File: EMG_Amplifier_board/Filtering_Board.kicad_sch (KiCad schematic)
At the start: 3 parts, among them U7 TPD2E001DRLR

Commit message: pcb design v1
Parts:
- removed R17, R18: 10R, Resistor_SMD:R_0402_1005Metric, symbol Device:R
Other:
- sheet DRL ports: added none; removed V_DD/2

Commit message: add capacitor to ESD
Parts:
- added C12: 0.1uF, Capacitor_SMD:C_0805_2012Metric, symbol Device:C_Small
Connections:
- net +V_DD: now also C12.2
- net GND: now also C12.1
- no-connect marks 0 -> 1
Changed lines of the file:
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@@
 		(color 0 0 0 0)
 	)
+	(junction
+		(at 110.49 152.4)
+		(diameter 0)
+		(color 0 0 0 0)
+	)
+	(no_connect
+		(at 101.6 142.24)
+	)
 	(wire
 		(pts
@@
 	(wire
 		(pts
+			(xy 110.49 154.94) (xy 110.49 152.4)
+		)
+		(stroke
+			(width 0)
+			(type default)
+		)
+	)
+	(wire
+		(pts
 			(xy 255.27 50.8) (xy 255.27 118.11)
 		)
@@
 	(wire
 		(pts
+			(xy 110.49 152.4) (xy 99.06 152.4)
+		)
+		(stroke
+			(width 0)
+			(type default)
+		)
+	)
+	(wire
+		(pts
 			(xy 163.83 45.72) (xy 121.92 45.72)
 		)
@@
 	(wire
 		(pts
+			(xy 110.49 160.02) (xy 110.49 161.29)
+		)
+		(stroke
+			(width 0)
+			(type default)
+		)
+	)
+	(wire
+		(pts
 			(xy 163.83 36.83) (xy 163.83 45.72)
 		)
@@
 	(wire
 		(pts
-			(xy 121.92 152.4) (xy 99.06 152.4)
+			(xy 121.92 152.4) (xy 110.49 152.4)
 		)
 		(stroke
@@
 					(unit 1)
 				)
+			)
+		)
+	)
+	(symbol
+		(lib_id "Device:C_Small")
+		(at 110.49 157.48 180)
+		(unit 1)
+		(exclude_from_sim no)
+		(in_bom yes)
+		(on_board yes)
+		(dnp no)
+		(property "Reference" "C12"
+			(at 104.902 160.02 0)
+			(effects
+				(font
+					(size 1.27 1.27)
+				)
+			)
+		)
+		(property "Value" "0.1uF"
+			(at 104.902 157.48 0)
+			(effects
+				(font
+					(size 1.27 1.27)
+				)
+			)
+		)
+		(property "Footprint" "Capacitor_SMD:C_0805_2012Metric"
+			(at 110.49 157.48 0)
+			(effects
+				(font
+					(size 1.27 1.27)
+				)
+				(hide yes)
+			)
+		)
+		(property "Datasheet" "~"
+			(at 110.49 157.48 0)
+			(effects
+				(font
+					(size 1.27 1.27)
+				)
+				(hide yes)
+			)
+		)
+		(property "Description" "Unpolarized capacitor, small symbol"
+			(at 110.49 157.48 0)
+			(effects
+				(font
+					(size 1.27 1.27)
+				)
+				(hide yes)
+			)
+		)
+		(pin "2"
+		)
+		(pin "1"
+		)
+		(instances
+			(project "EMG_amplifier"
+				(path "/26861adc-1ddf-4c37-9f8b-8db1c0839771/566a5450-97e0-4bc1-8c47-b0ac1397ab98"
+					(reference "C12")
+					(unit 1)
+				)
+			)
+		)
+	)
+	(symbol
+		(lib_id "power:GND")
+		(at 110.49 161.29 0)
+		(unit 1)
+		(exclude_from_sim no)
+		(in_bom yes)
+		(on_board yes)
+		(dnp no)
+		(fields_autoplaced yes)
+		(property "Reference" "#PWR020"
+			(at 110.49 167.64 0)
+			(effects
+				(font
+					(size 1.27 1.27)
+				)
+				(hide yes)
+			)
+		)
+		(property "Value" "GND"
+			(at 110.4899 165.1 90)
+			(effects
+				(font
+					(size 1.27 1.27)
+				)
+				(justify right)
+			)
+		)
+		(property "Footprint" ""
+			(at 110.49 161.29 0)
+			(effects
+				(font
+					(size 1.27 1.27)
+				)
+				(hide yes)
+			)
+		)
+		(property "Datasheet" ""
+			(at 110.49 161.29 0)
+			(effects
+				(font
+					(size 1.27 1.27)
+				)
+				(hide yes)
+			)
+		)
+		(property "Description" "Power symbol creates a global label with name \"GND\" , ground"
+			(at 110.49 161.29 0)
+			(effects
+				(font
+					(size 1.27 1.27)
+				)
+				(hide yes)
+			)
+		)
+		(pin "1"
+		)
+		(instances
+			(project "EMG_amplifier"
+				(path "/26861adc-1ddf-4c37-9f8b-8db1c0839771/566a5450-97e0-4bc1-8c47-b0ac1397ab98"
+					(reference "#PWR020")
+					(unit 1)
+				)

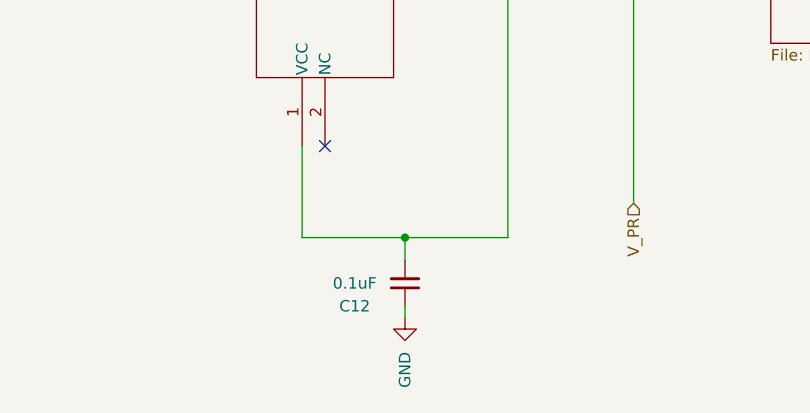
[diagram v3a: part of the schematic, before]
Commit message: replace 2012 capacitors with 1005
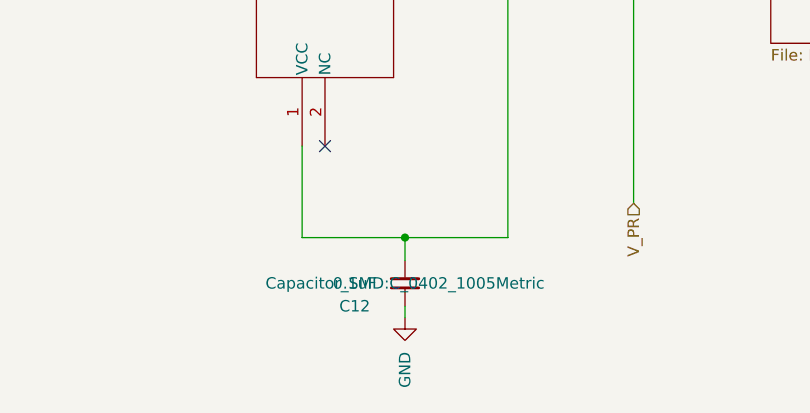
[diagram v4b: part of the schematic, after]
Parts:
- C12: footprint Capacitor_SMD:C_0805_2012Metric -> Capacitor_SMD:C_0402_1005Metric
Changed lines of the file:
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@@
 			)
 		)
-		(property "Footprint" "Capacitor_SMD:C_0805_2012Metric"
+		(property "Footprint" "Capacitor_SMD:C_0402_1005Metric"
 			(at 110.49 157.48 0)
 			(effects
@@
 					(size 1.27 1.27)
 				)
-				(hide yes)
 			)
 		)

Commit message: minor spacing changes
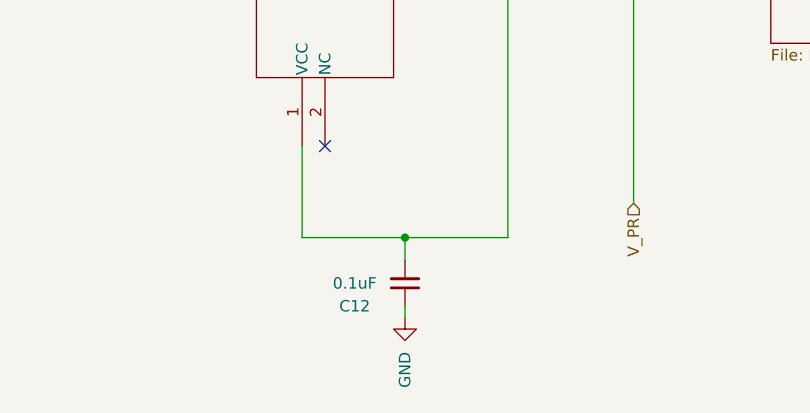
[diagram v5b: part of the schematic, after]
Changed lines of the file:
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@@
 					(size 1.27 1.27)
 				)
+				(hide yes)
 			)
 		)
